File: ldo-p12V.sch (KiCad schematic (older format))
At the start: 0 parts

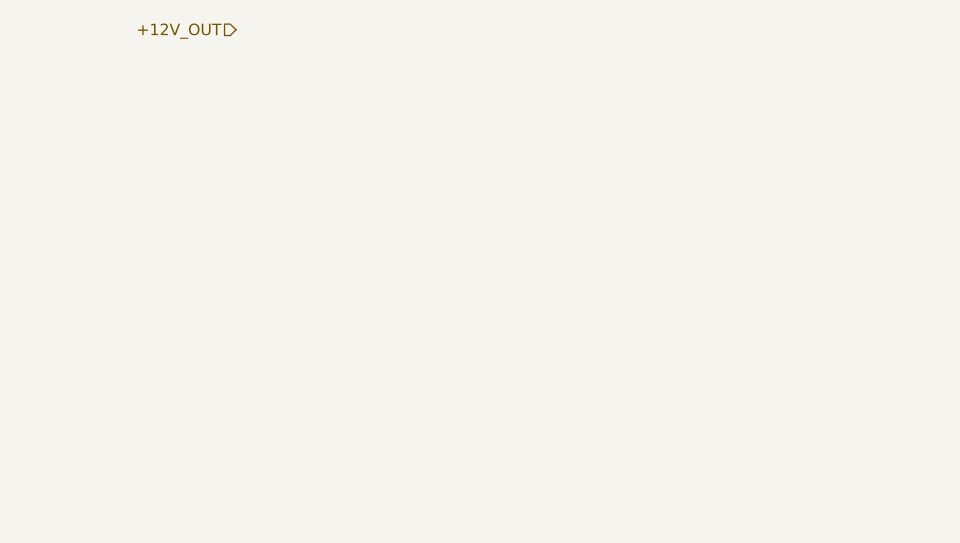
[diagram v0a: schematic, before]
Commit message: add schematics for LDO sheets
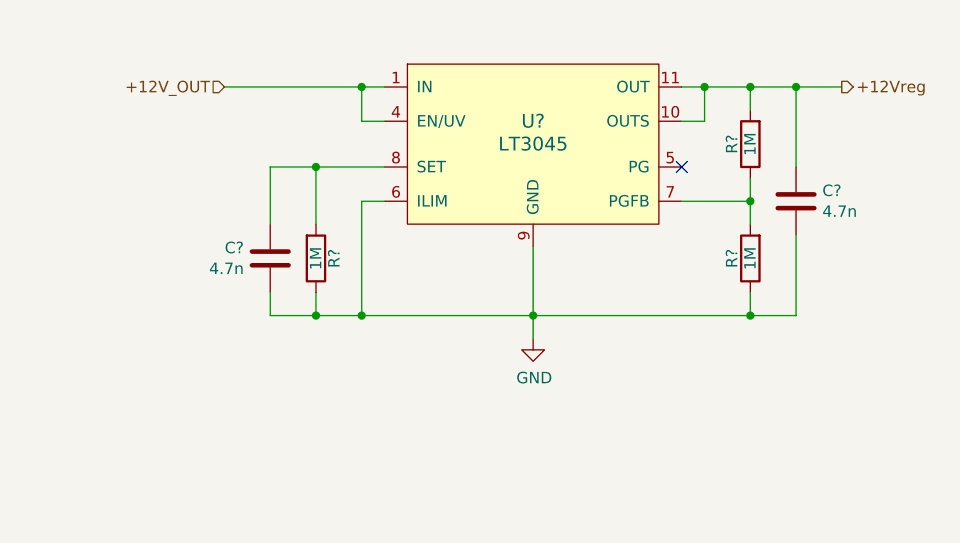
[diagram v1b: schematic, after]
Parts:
- added C? (x2): 4.7n, Capacitor_SMD:C_0805_2012Metric_Pad1.15x1.40mm_HandSolder, symbol Device:C
- added R? (x3): 1M, Resistor_SMD:R_0805_2012Metric_Pad1.15x1.40mm_HandSolder, symbol Device:R
- added U?: LT3045, Housings_SSOP:MSOP-12-1EP_3x4mm_Pitch0.65mm, symbol linear_technology:LT3045
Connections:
- new net: R?.1, R?.2, U?.7 (PGFB)
- new net: C?.2, R?.2, U?.8 (SET)
- new net +12Vreg: C?.2, R?.2, U?.10 (OUTS), U?.11 (OUT), U?.12 (OUT)
- new net GND: C?.1, C?.1, R?.1, R?.1, U?.13 (GND), U?.6 (ILIM), U?.9 (GND)
- new net IN: U?.1 (IN), U?.2 (IN), U?.3 (IN), U?.4 (EN/UV)
- no-connect marks 0 -> 1
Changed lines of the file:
@@
 Comment4 ""
 $EndDescr
-Text HLabel 4200 3400 0    50   Input ~ 0
+Text HLabel 4150 3650 0    50   Input ~ 0
 +12V_OUT
+$Comp
+L linear_technology:LT3045 U?
+U 1 1 5CA59434
+P 5500 3900
+F 0 "U?" H 5500 4000 60  0000 C CNN
+F 1 "LT3045" H 5500 3900 60  0000 C CNN
+F 2 "Housings_SSOP:MSOP-12-1EP_3x4mm_Pitch0.65mm" H 5500 4400 60  0001 C CNN
+F 3 "https://www.analog.com/media/en/technical-documentation/data-sheets/3045fa.pdf" H 5500 4300 60  0001 C CNN
+	1    5500 3900
+	1    0    0    -1
+$EndComp
+NoConn ~ 6150 4000
+$Comp
+L power:GND #PWR?
+U 1 1 5CA5C89F
+P 5500 4750
+AR Path="/5C903B7C/5CA5C89F" Ref="#PWR?"  Part="1"
+AR Path="/5CA59CF7/5CA5C89F" Ref="#PWR?"  Part="1"
+F 0 "#PWR?" H 5500 4500 50  0001 C CNN
+F 1 "GND" H 5505 4577 50  0000 C CNN
+F 2 "" H 5500 4750 50  0001 C CNN
+F 3 "" H 5500 4750 50  0001 C CNN
+	1    5500 4750
+	1    0    0    -1
+$EndComp
+Wire Wire Line
+	5500 4750 5500 4650
+Wire Wire Line
+	4850 4150 4750 4150
+Wire Wire Line
+	4750 4150 4750 4650
+Wire Wire Line
+	4750 4650 5500 4650
+Connection ~ 5500 4650
+Wire Wire Line
+	5500 4650 5500 4350
+Wire Wire Line
+	4150 3650 4750 3650
+Wire Wire Line
+	4750 3650 4750 3800
+Wire Wire Line
+	4750 3800 4850 3800
+Connection ~ 4750 3650
+Wire Wire Line
+	4750 3650 4850 3650
+$Comp
+L Device:R R?
+U 1 1 5CA5D410
+P 4550 4400
+AR Path="/5C87B3B6/5CA5D410" Ref="R?"  Part="1"
+AR Path="/5CA59CF7/5CA5D410" Ref="R?"  Part="1"
+F 0 "R?" V 4630 4400 50  0000 C CNN
+F 1 "1M" V 4550 4400 50  0000 C CNN
+F 2 "Resistor_SMD:R_0805_2012Metric_Pad1.15x1.40mm_HandSolder" V 4480 4400 50  0001 C CNN
+F 3 "https://industrial.panasonic.com/cdbs/www-data/pdf/RDA0000/AOA0000C304.pdf" H 4550 4400 50  0001 C CNN
+F 4 "RES SMD 1M OHM 1% 1/8W 0805" H 4550 4400 50  0001 C CNN "Description"
+F 5 "Panasonic Electronic Components" H 4550 4400 50  0001 C CNN "Manufacturer"
+F 6 "ERJ-6ENF1004V" H 4550 4400 50  0001 C CNN "Manufacturer Part Number"
+F 7 "Digi-Key" H 4550 4400 50  0001 C CNN "Supplier"
+F 8 "P1.00MCCT-ND" H 4550 4400 50  0001 C CNN "Supplier Part Number"
+	1    4550 4400
+	1    0    0    1
+$EndComp
+$Comp
+L Device:C C?
+U 1 1 5CA5D41C
+P 4350 4400
+AR Path="/5C87B3B6/5CA5D41C" Ref="C?"  Part="1"
+AR Path="/5CA59CF7/5CA5D41C" Ref="C?"  Part="1"
+F 0 "C?" H 4235 4354 50  0000 R CNN
+F 1 "4.7n" H 4235 4445 50  0000 R CNN
+F 2 "Capacitor_SMD:C_0805_2012Metric_Pad1.15x1.40mm_HandSolder" H 4388 4250 50  0001 C CNN
+F 3 "http://www.samsungsem.com/kr/support/product-search/mlcc/__icsFiles/afieldfile/2018/06/12/CL21C4R7BBANNNC.pdf" H 4350 4400 50  0001 C CNN
+F 4 "CAP CER 4.7PF 50V C0G/NP0 0805" H 1900 -750 50  0001 C CNN "Description"
+F 5 "Samsung Electro-Mechanics" H 1900 -750 50  0001 C CNN "Manufacturer"
+F 6 "CL21C4R7BBANNNC" H 1900 -750 50  0001 C CNN "Manufacturer Part Number"
+F 7 "Digi-Key" H 1900 -750 50  0001 C CNN "Supplier"
+F 8 "1276-1832-1-ND" H 1900 -750 50  0001 C CNN "Supplier Part Number"
+	1    4350 4400
+	1    0    0    1
+$EndComp
+Wire Wire Line
+	4850 4000 4550 4000
+Wire Wire Line
+	4350 4000 4350 4250
+Wire Wire Line
+	4550 4000 4550 4250
+Connection ~ 4550 4000
+Wire Wire Line
+	4550 4000 4350 4000
+Wire Wire Line
+	4350 4550 4350 4650
+Wire Wire Line
+	4350 4650 4550 4650
+Connection ~ 4750 4650
+Wire Wire Line
+	4550 4550 4550 4650
+Connection ~ 4550 4650
+Wire Wire Line
+	4550 4650 4750 4650
+$Comp
+L Device:R R?
+U 1 1 5CA5DD37
+P 6450 4400
+AR Path="/5C87B3B6/5CA5DD37" Ref="R?"  Part="1"
+AR Path="/5CA59CF7/5CA5DD37" Ref="R?"  Part="1"
+F 0 "R?" V 6530 4400 50  0000 C CNN
+F 1 "1M" V 6450 4400 50  0000 C CNN
+F 2 "Resistor_SMD:R_0805_2012Metric_Pad1.15x1.40mm_HandSolder" V 6380 4400 50  0001 C CNN
+F 3 "https://industrial.panasonic.com/cdbs/www-data/pdf/RDA0000/AOA0000C304.pdf" H 6450 4400 50  0001 C CNN
+F 4 "RES SMD 1M OHM 1% 1/8W 0805" H 6450 4400 50  0001 C CNN "Description"
+F 5 "Panasonic Electronic Components" H 6450 4400 50  0001 C CNN "Manufacturer"
+F 6 "ERJ-6ENF1004V" H 6450 4400 50  0001 C CNN "Manufacturer Part Number"
+F 7 "Digi-Key" H 6450 4400 50  0001 C CNN "Supplier"
+F 8 "P1.00MCCT-ND" H 6450 4400 50  0001 C CNN "Supplier Part Number"
+	1    6450 4400
+	-1   0    0    1
+$EndComp
+$Comp
+L Device:R R?
+U 1 1 5CA5DDF4
+P 6450 3900
+AR Path="/5C87B3B6/5CA5DDF4" Ref="R?"  Part="1"
+AR Path="/5CA59CF7/5CA5DDF4" Ref="R?"  Part="1"
+F 0 "R?" V 6530 3900 50  0000 C CNN
+F 1 "1M" V 6450 3900 50  0000 C CNN
+F 2 "Resistor_SMD:R_0805_2012Metric_Pad1.15x1.40mm_HandSolder" V 6380 3900 50  0001 C CNN
+F 3 "https://industrial.panasonic.com/cdbs/www-data/pdf/RDA0000/AOA0000C304.pdf" H 6450 3900 50  0001 C CNN
+F 4 "RES SMD 1M OHM 1% 1/8W 0805" H 6450 3900 50  0001 C CNN "Description"
+F 5 "Panasonic Electronic Components" H 6450 3900 50  0001 C CNN "Manufacturer"
+F 6 "ERJ-6ENF1004V" H 6450 3900 50  0001 C CNN "Manufacturer Part Number"
+F 7 "Digi-Key" H 6450 3900 50  0001 C CNN "Supplier"
+F 8 "P1.00MCCT-ND" H 6450 3900 50  0001 C CNN "Supplier Part Number"
+	1    6450 3900
+	-1   0    0    1
+$EndComp
+Wire Wire Line
+	6150 4150 6450 4150
+Wire Wire Line
+	6450 4150 6450 4050
+Wire Wire Line
+	6150 3650 6250 3650
+Wire Wire Line
+	6450 3650 6450 3750
+Wire Wire Line
+	6150 3800 6250 3800
+Wire Wire Line
+	6250 3800 6250 3650
+Connection ~ 6250 3650
+Wire Wire Line
+	6250 3650 6450 3650
+Wire Wire Line
+	6450 4150 6450 4250
+Connection ~ 6450 4150
+Wire Wire Line
+	6450 4550 6450 4650
+Wire Wire Line
+	6450 4650 5500 4650
+$Comp
+L Device:C C?
+U 1 1 5CA5F77A
+P 6650 4150
+AR Path="/5C87B3B6/5CA5F77A" Ref="C?"  Part="1"
+AR Path="/5CA59CF7/5CA5F77A" Ref="C?"  Part="1"
+F 0 "C?" H 6535 4104 50  0000 R CNN
+F 1 "4.7n" H 6535 4195 50  0000 R CNN
+F 2 "Capacitor_SMD:C_0805_2012Metric_Pad1.15x1.40mm_HandSolder" H 6688 4000 50  0001 C CNN
+F 3 "http://www.samsungsem.com/kr/support/product-search/mlcc/__icsFiles/afieldfile/2018/06/12/CL21C4R7BBANNNC.pdf" H 6650 4150 50  0001 C CNN
+F 4 "CAP CER 4.7PF 50V C0G/NP0 0805" H 4200 -1000 50  0001 C CNN "Description"
+F 5 "Samsung Electro-Mechanics" H 4200 -1000 50  0001 C CNN "Manufacturer"
+F 6 "CL21C4R7BBANNNC" H 4200 -1000 50  0001 C CNN "Manufacturer Part Number"
+F 7 "Digi-Key" H 4200 -1000 50  0001 C CNN "Supplier"
+F 8 "1276-1832-1-ND" H 4200 -1000 50  0001 C CNN "Supplier Part Number"
+	1    6650 4150
+	-1   0    0    1
+$EndComp
+Wire Wire Line
+	6450 3650 6650 3650
+Wire Wire Line
+	6650 3650 6650 4000
+Connection ~ 6450 3650
+Wire Wire Line
+	6650 4300 6650 4650
+Wire Wire Line
+	6650 4650 6450 4650
+Connection ~ 6450 4650
+Text HLabel 6850 3650 2    50   Output ~ 0
++12Vreg
+Wire Wire Line
+	6850 3650 6650 3650
+Connection ~ 6650 3650
 $EndSCHEMATC

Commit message: update schematic after LTSpice simulations
- enable EN/UV and PGFB usage for LDOs
  - PGFB required for fast startup
  - EN/UV required to allow boost to ramp up
- take care of some TODOs in usbc-power sch
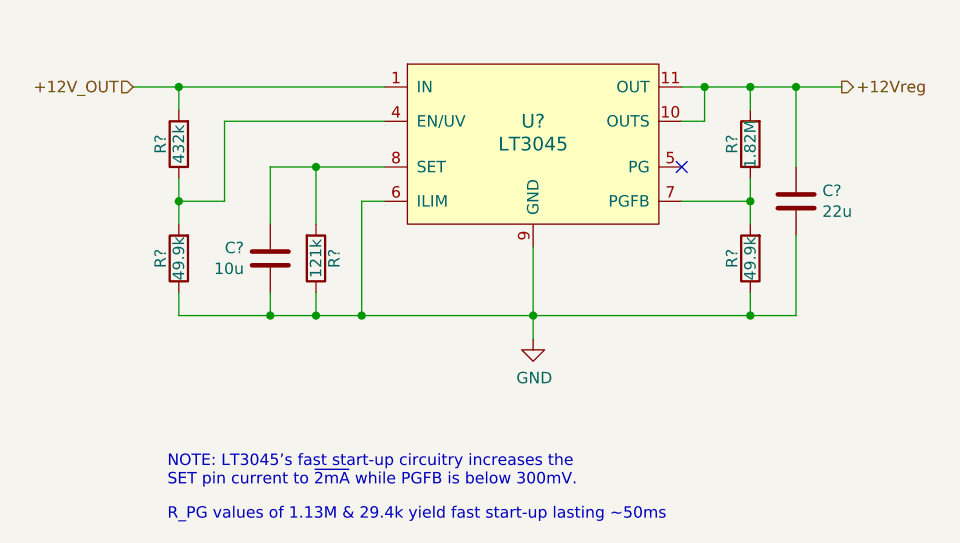
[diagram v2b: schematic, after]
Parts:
- added R?: 49.9k, Resistor_SMD:R_0805_2012Metric_Pad1.15x1.40mm_HandSolder, symbol Device:R
- added R?: 432k, Resistor_SMD:R_0805_2012Metric_Pad1.15x1.40mm_HandSolder, symbol Device:R
- C?: value 4.7n -> 10u
- C?: value 4.7n -> 22u
- R?: value 1M -> 121k
- R?: value 1M -> 49.9k
- R?: value 1M -> 1.82M
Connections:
- net GND: now also R?.1
- net IN: now also R?.2; no longer U?.4 (EN/UV)
- new net: R?.1, R?.2, U?.4 (EN/UV)
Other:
- note added: "NOTE: LT3045’s fast start-up circuitry increases the\nSET pin current to ~2mA while PGFB is below 300mV."
- note added: "R_PG values of 1.13M & 29.4k yield fast start-up lasting ~~50ms"
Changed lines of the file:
@@
 Comment4 ""
 $EndDescr
-Text HLabel 4150 3650 0    50   Input ~ 0
+Text HLabel 3750 3650 0    50   Input ~ 0
 +12V_OUT
 $Comp
@@
 Wire Wire Line
 	5500 4650 5500 4350
-Wire Wire Line
-	4150 3650 4750 3650
-Wire Wire Line
-	4750 3650 4750 3800
-Wire Wire Line
-	4750 3800 4850 3800
-Connection ~ 4750 3650
-Wire Wire Line
-	4750 3650 4850 3650
 $Comp
 L Device:R R?
@@
 AR Path="/5CA59CF7/5CA5D410" Ref="R?"  Part="1"
 F 0 "R?" V 4630 4400 50  0000 C CNN
-F 1 "1M" V 4550 4400 50  0000 C CNN
+F 1 "121k" V 4550 4400 50  0000 C CNN
 F 2 "Resistor_SMD:R_0805_2012Metric_Pad1.15x1.40mm_HandSolder" V 4480 4400 50  0001 C CNN
 F 3 "https://industrial.panasonic.com/cdbs/www-data/pdf/RDA0000/AOA0000C304.pdf" H 4550 4400 50  0001 C CNN
@@
 AR Path="/5CA59CF7/5CA5D41C" Ref="C?"  Part="1"
 F 0 "C?" H 4235 4354 50  0000 R CNN
-F 1 "4.7n" H 4235 4445 50  0000 R CNN
+F 1 "10u" H 4235 4445 50  0000 R CNN
 F 2 "Capacitor_SMD:C_0805_2012Metric_Pad1.15x1.40mm_HandSolder" H 4388 4250 50  0001 C CNN
 F 3 "http://www.samsungsem.com/kr/support/product-search/mlcc/__icsFiles/afieldfile/2018/06/12/CL21C4R7BBANNNC.pdf" H 4350 4400 50  0001 C CNN
@@
 AR Path="/5CA59CF7/5CA5DD37" Ref="R?"  Part="1"
 F 0 "R?" V 6530 4400 50  0000 C CNN
-F 1 "1M" V 6450 4400 50  0000 C CNN
+F 1 "49.9k" V 6450 4400 50  0000 C CNN
 F 2 "Resistor_SMD:R_0805_2012Metric_Pad1.15x1.40mm_HandSolder" V 6380 4400 50  0001 C CNN
 F 3 "https://industrial.panasonic.com/cdbs/www-data/pdf/RDA0000/AOA0000C304.pdf" H 6450 4400 50  0001 C CNN
@@
 AR Path="/5CA59CF7/5CA5DDF4" Ref="R?"  Part="1"
 F 0 "R?" V 6530 3900 50  0000 C CNN
-F 1 "1M" V 6450 3900 50  0000 C CNN
+F 1 "1.82M" V 6450 3900 50  0000 C CNN
 F 2 "Resistor_SMD:R_0805_2012Metric_Pad1.15x1.40mm_HandSolder" V 6380 3900 50  0001 C CNN
 F 3 "https://industrial.panasonic.com/cdbs/www-data/pdf/RDA0000/AOA0000C304.pdf" H 6450 3900 50  0001 C CNN
@@
 AR Path="/5CA59CF7/5CA5F77A" Ref="C?"  Part="1"
 F 0 "C?" H 6535 4104 50  0000 R CNN
-F 1 "4.7n" H 6535 4195 50  0000 R CNN
+F 1 "22u" H 6535 4195 50  0000 R CNN
 F 2 "Capacitor_SMD:C_0805_2012Metric_Pad1.15x1.40mm_HandSolder" H 6688 4000 50  0001 C CNN
 F 3 "http://www.samsungsem.com/kr/support/product-search/mlcc/__icsFiles/afieldfile/2018/06/12/CL21C4R7BBANNNC.pdf" H 6650 4150 50  0001 C CNN
@@
 	6850 3650 6650 3650
 Connection ~ 6650 3650
+Text Notes 3900 5400 0    50   ~ 0
+NOTE: LT3045’s fast start-up circuitry increases the\nSET pin current to ~2mA while PGFB is below 300mV.
+Text Notes 3900 5550 0    50   ~ 0
+R_PG values of 1.13M & 29.4k yield fast start-up lasting ~~50ms
+$Comp
+L Device:R R?
+U 1 1 5CAC0D09
+P 3950 4400
+AR Path="/5C87B3B6/5CAC0D09" Ref="R?"  Part="1"
+AR Path="/5CA59CF7/5CAC0D09" Ref="R?"  Part="1"
+F 0 "R?" V 4030 4400 50  0000 C CNN
+F 1 "49.9k" V 3950 4400 50  0000 C CNN
+F 2 "Resistor_SMD:R_0805_2012Metric_Pad1.15x1.40mm_HandSolder" V 3880 4400 50  0001 C CNN
+F 3 "https://industrial.panasonic.com/cdbs/www-data/pdf/RDA0000/AOA0000C304.pdf" H 3950 4400 50  0001 C CNN
+F 4 "RES SMD 1M OHM 1% 1/8W 0805" H 3950 4400 50  0001 C CNN "Description"
+F 5 "Panasonic Electronic Components" H 3950 4400 50  0001 C CNN "Manufacturer"
+F 6 "ERJ-6ENF1004V" H 3950 4400 50  0001 C CNN "Manufacturer Part Number"
+F 7 "Digi-Key" H 3950 4400 50  0001 C CNN "Supplier"
+F 8 "P1.00MCCT-ND" H 3950 4400 50  0001 C CNN "Supplier Part Number"
+	1    3950 4400
+	-1   0    0    1
+$EndComp
+$Comp
+L Device:R R?
+U 1 1 5CAC0D15
+P 3950 3900
+AR Path="/5C87B3B6/5CAC0D15" Ref="R?"  Part="1"
+AR Path="/5CA59CF7/5CAC0D15" Ref="R?"  Part="1"
+F 0 "R?" V 4030 3900 50  0000 C CNN
+F 1 "432k" V 3950 3900 50  0000 C CNN
+F 2 "Resistor_SMD:R_0805_2012Metric_Pad1.15x1.40mm_HandSolder" V 3880 3900 50  0001 C CNN
+F 3 "https://industrial.panasonic.com/cdbs/www-data/pdf/RDA0000/AOA0000C304.pdf" H 3950 3900 50  0001 C CNN
+F 4 "RES SMD 1M OHM 1% 1/8W 0805" H 3950 3900 50  0001 C CNN "Description"
+F 5 "Panasonic Electronic Components" H 3950 3900 50  0001 C CNN "Manufacturer"
+F 6 "ERJ-6ENF1004V" H 3950 3900 50  0001 C CNN "Manufacturer Part Number"
+F 7 "Digi-Key" H 3950 3900 50  0001 C CNN "Supplier"
+F 8 "P1.00MCCT-ND" H 3950 3900 50  0001 C CNN "Supplier Part Number"
+	1    3950 3900
+	-1   0    0    1
+$EndComp
+Wire Wire Line
+	3950 3650 3950 3750
+Wire Wire Line
+	3950 4550 3950 4650
+Wire Wire Line
+	3950 4050 3950 4150
+Wire Wire Line
+	3750 3650 3950 3650
+Connection ~ 3950 3650
+Wire Wire Line
+	3950 3650 4850 3650
+Wire Wire Line
+	4850 3800 4150 3800
+Wire Wire Line
+	4150 3800 4150 4150
+Wire Wire Line
+	4150 4150 3950 4150
+Connection ~ 3950 4150
+Wire Wire Line
+	3950 4150 3950 4250
+Wire Wire Line
+	3950 4650 4350 4650
+Connection ~ 4350 4650
 $EndSCHEMATC

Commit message: remove false desc for copied resistors in ldo schematics
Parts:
- C? (x2): Description CAP CER 4.7PF 50V C0G/NP0 0805 -> (none)
- R? (x5): Description RES SMD 1M OHM 1% 1/8W 0805 -> (none)
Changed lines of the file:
@@
 F 2 "Resistor_SMD:R_0805_2012Metric_Pad1.15x1.40mm_HandSolder" V 4480 4400 50  0001 C CNN
 F 3 "https://industrial.panasonic.com/cdbs/www-data/pdf/RDA0000/AOA0000C304.pdf" H 4550 4400 50  0001 C CNN
-F 4 "RES SMD 1M OHM 1% 1/8W 0805" H 4550 4400 50  0001 C CNN "Description"
+F 4 "" H 4550 4400 50  0001 C CNN "Description"
 F 5 "Panasonic Electronic Components" H 4550 4400 50  0001 C CNN "Manufacturer"
 F 6 "ERJ-6ENF1004V" H 4550 4400 50  0001 C CNN "Manufacturer Part Number"
@@
 F 2 "Capacitor_SMD:C_0805_2012Metric_Pad1.15x1.40mm_HandSolder" H 4388 4250 50  0001 C CNN
 F 3 "http://www.samsungsem.com/kr/support/product-search/mlcc/__icsFiles/afieldfile/2018/06/12/CL21C4R7BBANNNC.pdf" H 4350 4400 50  0001 C CNN
-F 4 "CAP CER 4.7PF 50V C0G/NP0 0805" H 1900 -750 50  0001 C CNN "Description"
+F 4 "" H 1900 -750 50  0001 C CNN "Description"
 F 5 "Samsung Electro-Mechanics" H 1900 -750 50  0001 C CNN "Manufacturer"
 F 6 "CL21C4R7BBANNNC" H 1900 -750 50  0001 C CNN "Manufacturer Part Number"
@@
 F 2 "Resistor_SMD:R_0805_2012Metric_Pad1.15x1.40mm_HandSolder" V 6380 4400 50  0001 C CNN
 F 3 "https://industrial.panasonic.com/cdbs/www-data/pdf/RDA0000/AOA0000C304.pdf" H 6450 4400 50  0001 C CNN
-F 4 "RES SMD 1M OHM 1% 1/8W 0805" H 6450 4400 50  0001 C CNN "Description"
+F 4 "" H 6450 4400 50  0001 C CNN "Description"
 F 5 "Panasonic Electronic Components" H 6450 4400 50  0001 C CNN "Manufacturer"
 F 6 "ERJ-6ENF1004V" H 6450 4400 50  0001 C CNN "Manufacturer Part Number"
@@
 F 2 "Resistor_SMD:R_0805_2012Metric_Pad1.15x1.40mm_HandSolder" V 6380 3900 50  0001 C CNN
 F 3 "https://industrial.panasonic.com/cdbs/www-data/pdf/RDA0000/AOA0000C304.pdf" H 6450 3900 50  0001 C CNN
-F 4 "RES SMD 1M OHM 1% 1/8W 0805" H 6450 3900 50  0001 C CNN "Description"
+F 4 "" H 6450 3900 50  0001 C CNN "Description"
 F 5 "Panasonic Electronic Components" H 6450 3900 50  0001 C CNN "Manufacturer"
 F 6 "ERJ-6ENF1004V" H 6450 3900 50  0001 C CNN "Manufacturer Part Number"
@@
 F 2 "Capacitor_SMD:C_0805_2012Metric_Pad1.15x1.40mm_HandSolder" H 6688 4000 50  0001 C CNN
 F 3 "http://www.samsungsem.com/kr/support/product-search/mlcc/__icsFiles/afieldfile/2018/06/12/CL21C4R7BBANNNC.pdf" H 6650 4150 50  0001 C CNN
-F 4 "CAP CER 4.7PF 50V C0G/NP0 0805" H 4200 -1000 50  0001 C CNN "Description"
+F 4 "" H 4200 -1000 50  0001 C CNN "Description"
 F 5 "Samsung Electro-Mechanics" H 4200 -1000 50  0001 C CNN "Manufacturer"
 F 6 "CL21C4R7BBANNNC" H 4200 -1000 50  0001 C CNN "Manufacturer Part Number"
@@
 F 2 "Resistor_SMD:R_0805_2012Metric_Pad1.15x1.40mm_HandSolder" V 3880 4400 50  0001 C CNN
 F 3 "https://industrial.panasonic.com/cdbs/www-data/pdf/RDA0000/AOA0000C304.pdf" H 3950 4400 50  0001 C CNN
-F 4 "RES SMD 1M OHM 1% 1/8W 0805" H 3950 4400 50  0001 C CNN "Description"
+F 4 "" H 3950 4400 50  0001 C CNN "Description"
 F 5 "Panasonic Electronic Components" H 3950 4400 50  0001 C CNN "Manufacturer"
 F 6 "ERJ-6ENF1004V" H 3950 4400 50  0001 C CNN "Manufacturer Part Number"
@@
 F 2 "Resistor_SMD:R_0805_2012Metric_Pad1.15x1.40mm_HandSolder" V 3880 3900 50  0001 C CNN
 F 3 "https://industrial.panasonic.com/cdbs/www-data/pdf/RDA0000/AOA0000C304.pdf" H 3950 3900 50  0001 C CNN
-F 4 "RES SMD 1M OHM 1% 1/8W 0805" H 3950 3900 50  0001 C CNN "Description"
+F 4 "" H 3950 3900 50  0001 C CNN "Description"
 F 5 "Panasonic Electronic Components" H 3950 3900 50  0001 C CNN "Manufacturer"
 F 6 "ERJ-6ENF1004V" H 3950 3900 50  0001 C CNN "Manufacturer Part Number"

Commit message: update hierarchal pin names to be accurate to new settings
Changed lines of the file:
@@
 $EndDescr
 Text HLabel 3750 3650 0    50   Input ~ 0
-+12V_OUT
++13V_IN
 $Comp
 L linear_technology:LT3045 U?
